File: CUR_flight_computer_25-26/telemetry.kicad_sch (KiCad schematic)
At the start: 19 parts, among them J14 Conn_Coaxial_Small, U5 E22-400MM_22S

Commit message: Apply MPNs for capacitors and connectors
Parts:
- C25: MPN (none) -> C0603C105K4RACTU
- C26, C27: value C_Small -> DNP; now not fitted; now left out of the parts list
- J14: value Conn_Coaxial_Small -> CON-SMA-EDGE-S; MPN (none) -> CON-SMA-EDGE-S
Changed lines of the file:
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@@
+			)
+		)
+		(property "MPN" "C0603C105K4RACTU"
+			(at 63.5 36.83 0)
+			(effects
+				(font
+					(size 1.27 1.27)
+				)
 			)
 		)
@@
 		(unit 1)
 		(exclude_from_sim no)
-		(in_bom yes)
-		(on_board yes)
-		(dnp no)
+		(in_bom no)
+		(on_board yes)
+		(dnp yes)
 		(fields_autoplaced yes)
 		(property "Reference" "C26"
@@
 			)
 		)
-		(property "Value" "C_Small"
+		(property "Value" "DNP"
 			(at 107.95 54.6162 0)
 			(effects
@@
 		(unit 1)
 		(exclude_from_sim no)
-		(in_bom yes)
-		(on_board yes)
-		(dnp no)
+		(in_bom no)
+		(on_board yes)
+		(dnp yes)
 		(fields_autoplaced yes)
 		(property "Reference" "C27"
@@
 			)
 		)
-		(property "Value" "C_Small"
+		(property "Value" "DNP"
 			(at 121.92 54.6162 0)
 			(effects
@@
 			)
 		)
-		(property "Value" "Conn_Coaxial_Small"
+		(property "Value" "CON-SMA-EDGE-S"
 			(at 130.2904 45.72 0)
 			(effects
@@
 			)
 		)
+		(property "MPN" "CON-SMA-EDGE-S"
+			(at 130.81 49.53 0)
+			(effects
+				(font
+					(size 1.27 1.27)
+				)
+			)
+		)

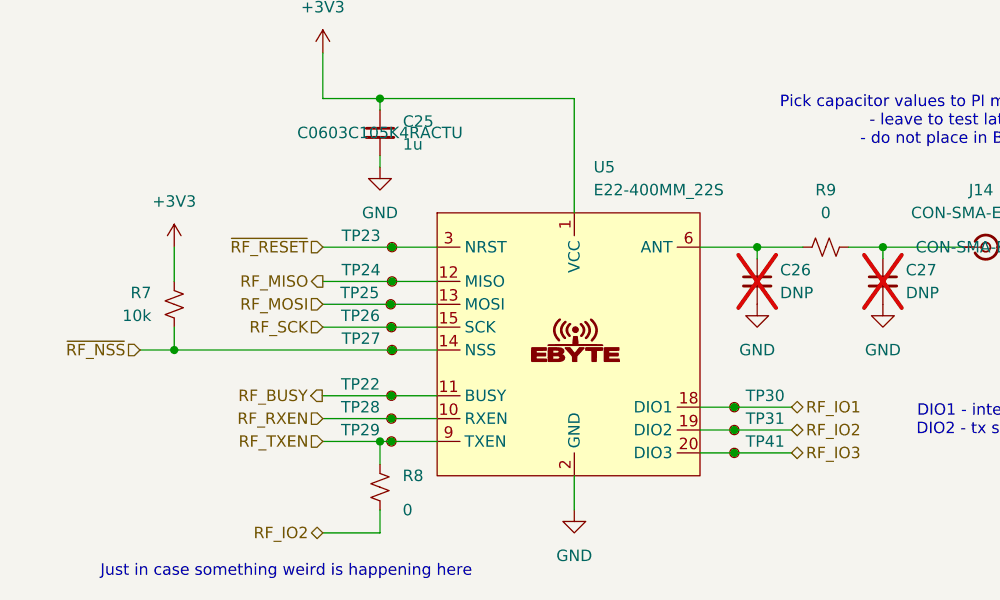
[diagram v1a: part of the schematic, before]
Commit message: Add MPNs for ICs
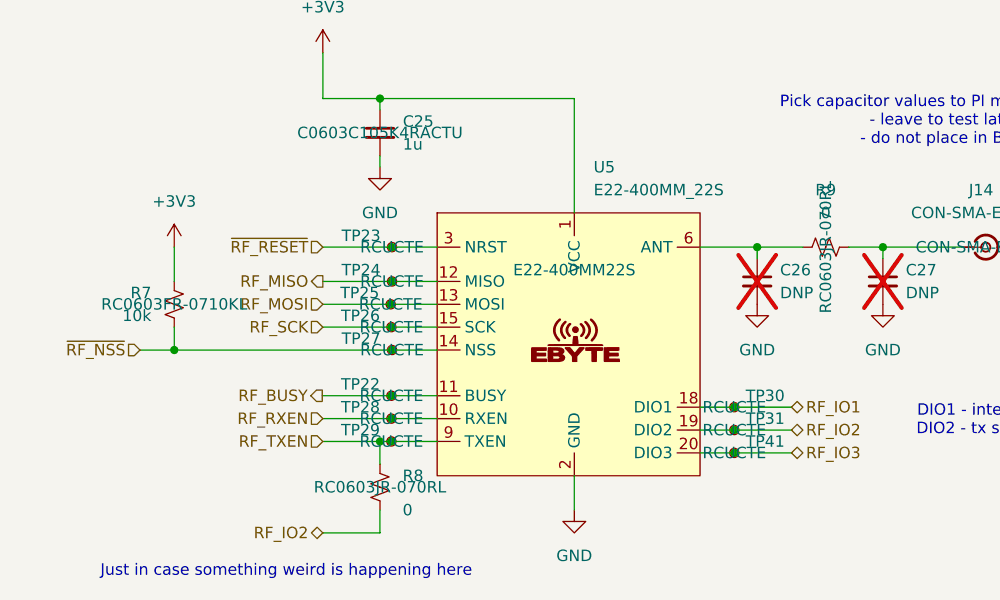
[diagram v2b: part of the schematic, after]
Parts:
- R7: MPN (none) -> RC0603FR-0710KL
- R8, R9: MPN (none) -> RC0603JR-070RL
- TP22, TP23, TP24, TP25, TP26, TP27, TP28, TP29, TP30, TP31, TP41: value TestPoint_Small -> RCUCTE; MPN (none) -> RCUCTE
- U5: MPN (none) -> E22-400MM22S
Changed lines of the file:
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@@
 			)
 		)
-		(property "Value" "TestPoint_Small"
+		(property "Value" "RCUCTE"
 			(at 63.5679 50.7999 0)
 			(effects
@@
 				)
 				(hide yes)
+			)
+		)
+		(property "MPN" "RCUCTE"
+			(at 64.8379 49.53 0)
+			(effects
+				(font
+					(size 1.27 1.27)
+				)
 			)
 		)
@@
 			)
 		)
-		(property "Value" "TestPoint_Small"
+		(property "Value" "RCUCTE"
 			(at 63.5 59.6899 0)
 			(effects
@@
 				)
 				(hide yes)
+			)
+		)
+		(property "MPN" "RCUCTE"
+			(at 64.77 58.42 0)
+			(effects
+				(font
+					(size 1.27 1.27)
+				)
 			)
 		)
@@
 			)
 		)
-		(property "Value" "TestPoint_Small"
+		(property "Value" "RCUCTE"
 			(at 63.5 67.3099 0)
 			(effects
@@
 				)
 				(hide yes)
+			)
+		)
+		(property "MPN" "RCUCTE"
+			(at 64.77 66.04 0)
+			(effects
+				(font
+					(size 1.27 1.27)
+				)
 			)
 		)
@@
 			)
 		)
-		(property "Value" "TestPoint_Small"
+		(property "Value" "RCUCTE"
 			(at 63.5 72.3899 0)
 			(effects
@@
 				)
 				(hide yes)
+			)
+		)
+		(property "MPN" "RCUCTE"
+			(at 64.77 71.12 0)
+			(effects
+				(font
+					(size 1.27 1.27)
+				)
 			)
 		)
@@
 			)
 		)
+		(property "MPN" "RC0603JR-070RL"
+			(at 63.5 76.2 0)
+			(effects
+				(font
+					(size 1.27 1.27)
+				)
+			)
+		)
 		(pin "1"
 		)
@@
 			)
 		)
-		(property "Value" "TestPoint_Small"
+		(property "Value" "RCUCTE"
 			(at 63.5 69.8499 0)
 			(effects
@@
 				)
 				(hide yes)
+			)
+		)
+		(property "MPN" "RCUCTE"
+			(at 64.77 68.58 0)
+			(effects
+				(font
+					(size 1.27 1.27)
+				)
 			)
 		)
@@
 			)
 		)
-		(property "Value" "TestPoint_Small"
+		(property "Value" "RCUCTE"
 			(at 104.14 71.1199 0)
 			(effects
@@
 			)
 		)
+		(property "MPN" "RCUCTE"
+			(at 102.87 69.85 0)
+			(effects
+				(font
+					(size 1.27 1.27)
+				)
+			)
+		)
 		(pin "1"
 		)
@@
 			)
 		)
-		(property "Value" "TestPoint_Small"
+		(property "Value" "RCUCTE"
 			(at 104.14 73.6599 0)
 			(effects
@@
 			)
 		)
+		(property "MPN" "RCUCTE"
+			(at 102.87 72.39 0)
+			(effects
+				(font
+					(size 1.27 1.27)
+				)
+			)
+		)
 		(pin "1"
 		)
@@
 			)
 		)
+		(property "MPN" "RC0603JR-070RL"
+			(at 113.03 49.53 0)
+			(effects
+				(font
+					(size 1.27 1.27)
+				)
+			)
+		)
 		(pin "1"
 		)
@@
 				)
 				(hide yes)
+			)
+		)
+		(property "MPN" "E22-400MM22S"
+			(at 85.09 52.07 0)
+			(effects
+				(font
+					(size 1.27 1.27)
+				)
 			)
 		)
@@
 			)
 		)
-		(property "Value" "TestPoint_Small"
+		(property "Value" "RCUCTE"
 			(at 63.5679 54.6099 0)
 			(effects
@@
 				)
 				(hide yes)
+			)
+		)
+		(property "MPN" "RCUCTE"
+			(at 64.8379 53.34 0)
+			(effects
+				(font
+					(size 1.27 1.27)
+				)
 			)
 		)
@@
 			)
 		)
-		(property "Value" "TestPoint_Small"
+		(property "Value" "RCUCTE"
 			(at 63.423 57.1499 0)
 			(effects
@@
 			)
 		)
+		(property "MPN" "RCUCTE"
+			(at 64.693 55.88 0)
+			(effects
+				(font
+					(size 1.27 1.27)
+				)
+			)
+		)
 		(pin "1"
 		)
@@
 			)
 		)
-		(property "Value" "TestPoint_Small"
+		(property "Value" "RCUCTE"
 			(at 104.14 68.5799 0)
 			(effects
@@
 			)
 		)
+		(property "MPN" "RCUCTE"
+			(at 102.87 67.31 0)
+			(effects
+				(font
+					(size 1.27 1.27)
+				)
+			)
+		)
 		(pin "1"
 		)
@@
 				)
 				(hide yes)
+			)
+		)
+		(property "MPN" "RC0603FR-0710KL"
+			(at 40.64 55.88 0)
+			(effects
+				(font
+					(size 1.27 1.27)
+				)
 			)
 		)
@@
 			)
 		)
-		(property "Value" "TestPoint_Small"
+		(property "Value" "RCUCTE"
 			(at 63.5679 62.2299 0)
 			(effects
@@
 			)
 		)
+		(property "MPN" "RCUCTE"
+			(at 64.8379 60.96 0)
+			(effects
+				(font
+					(size 1.27 1.27)
+				)
+			)
+		)

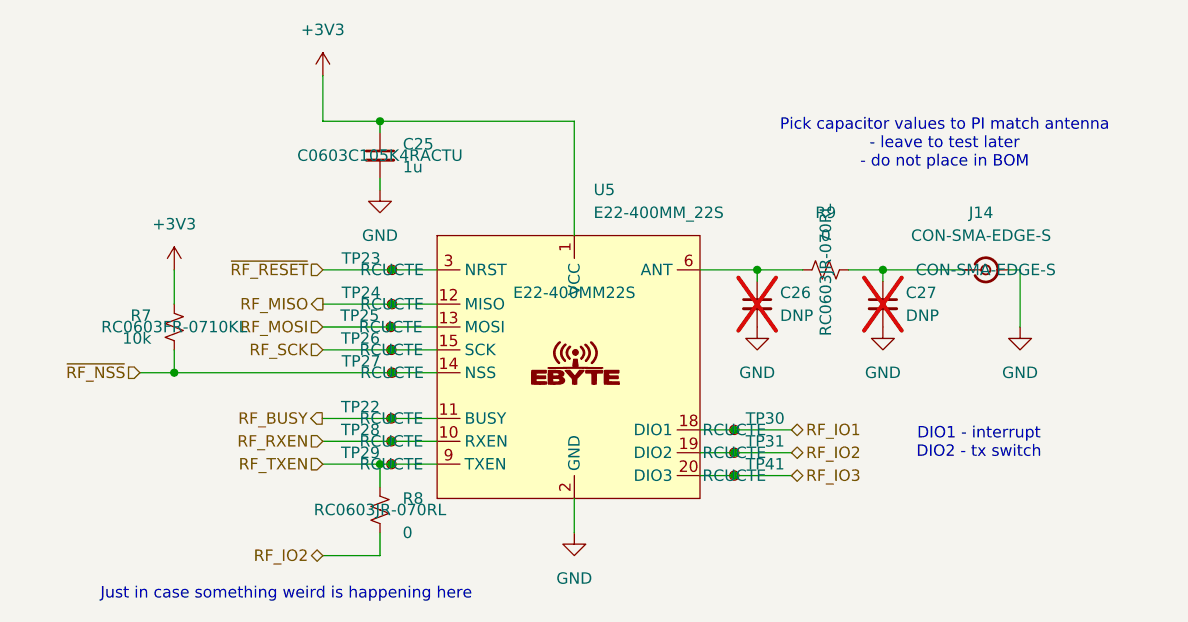
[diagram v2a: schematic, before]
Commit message: Hide MPNs
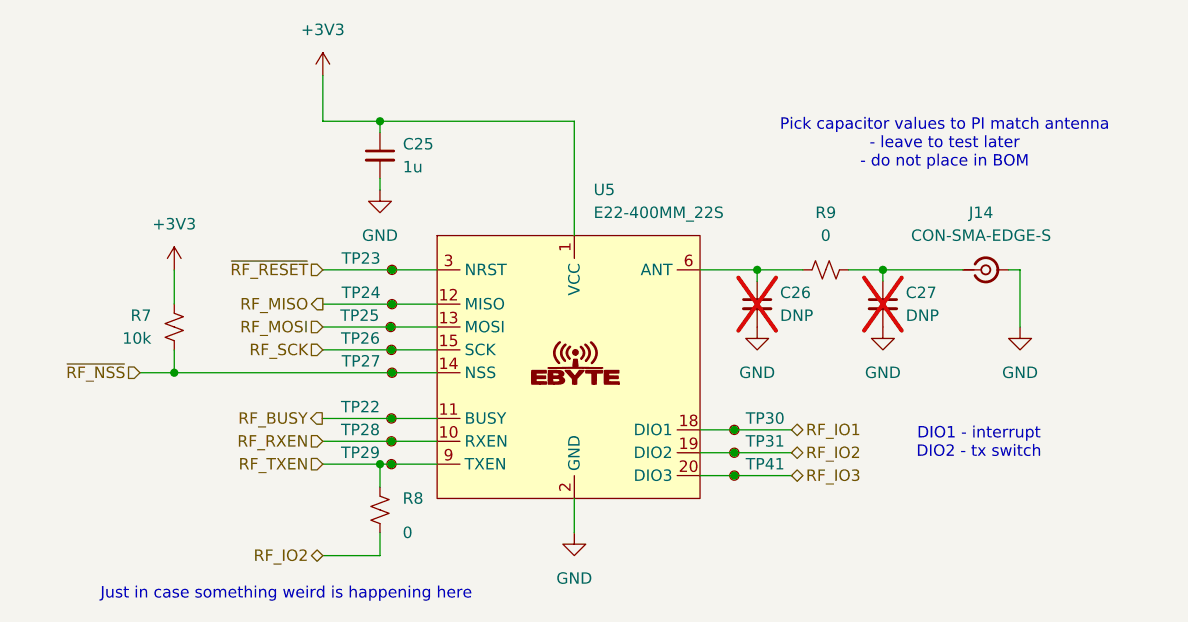
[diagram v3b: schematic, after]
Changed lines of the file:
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@@
 					(size 1.27 1.27)
 				)
+				(hide yes)
 			)
 		)
@@
 					(size 1.27 1.27)
 				)
+				(hide yes)
 			)
 		)
@@
 					(size 1.27 1.27)
 				)
+				(hide yes)
 			)
 		)
@@
 					(size 1.27 1.27)
 				)
+				(hide yes)
 			)
 		)
@@
 					(size 1.27 1.27)
 				)
+				(hide yes)
 			)
 		)
@@
 					(size 1.27 1.27)
 				)
+				(hide yes)
 			)
 		)
@@
 					(size 1.27 1.27)
 				)
+				(hide yes)
 			)
 		)
@@
 					(size 1.27 1.27)
 				)
+				(hide yes)
 			)
 		)
@@
 					(size 1.27 1.27)
 				)
+				(hide yes)
 			)
 		)
@@
 					(size 1.27 1.27)
 				)
+				(hide yes)
 			)
 		)
@@
 					(size 1.27 1.27)
 				)
+				(hide yes)
 			)
 		)
@@
 					(size 1.27 1.27)
 				)
+				(hide yes)
 			)
 		)
@@
 					(size 1.27 1.27)
 				)
+				(hide yes)
 			)
 		)
@@
 					(size 1.27 1.27)
 				)
+				(hide yes)
 			)
 		)
@@
 					(size 1.27 1.27)
 				)
+				(hide yes)
 			)
 		)
@@
 					(size 1.27 1.27)
 				)
+				(hide yes)
 			)
 		)
@@
 					(size 1.27 1.27)
 				)
-			)
-		)
+				(hide yes)
+			)
+		)

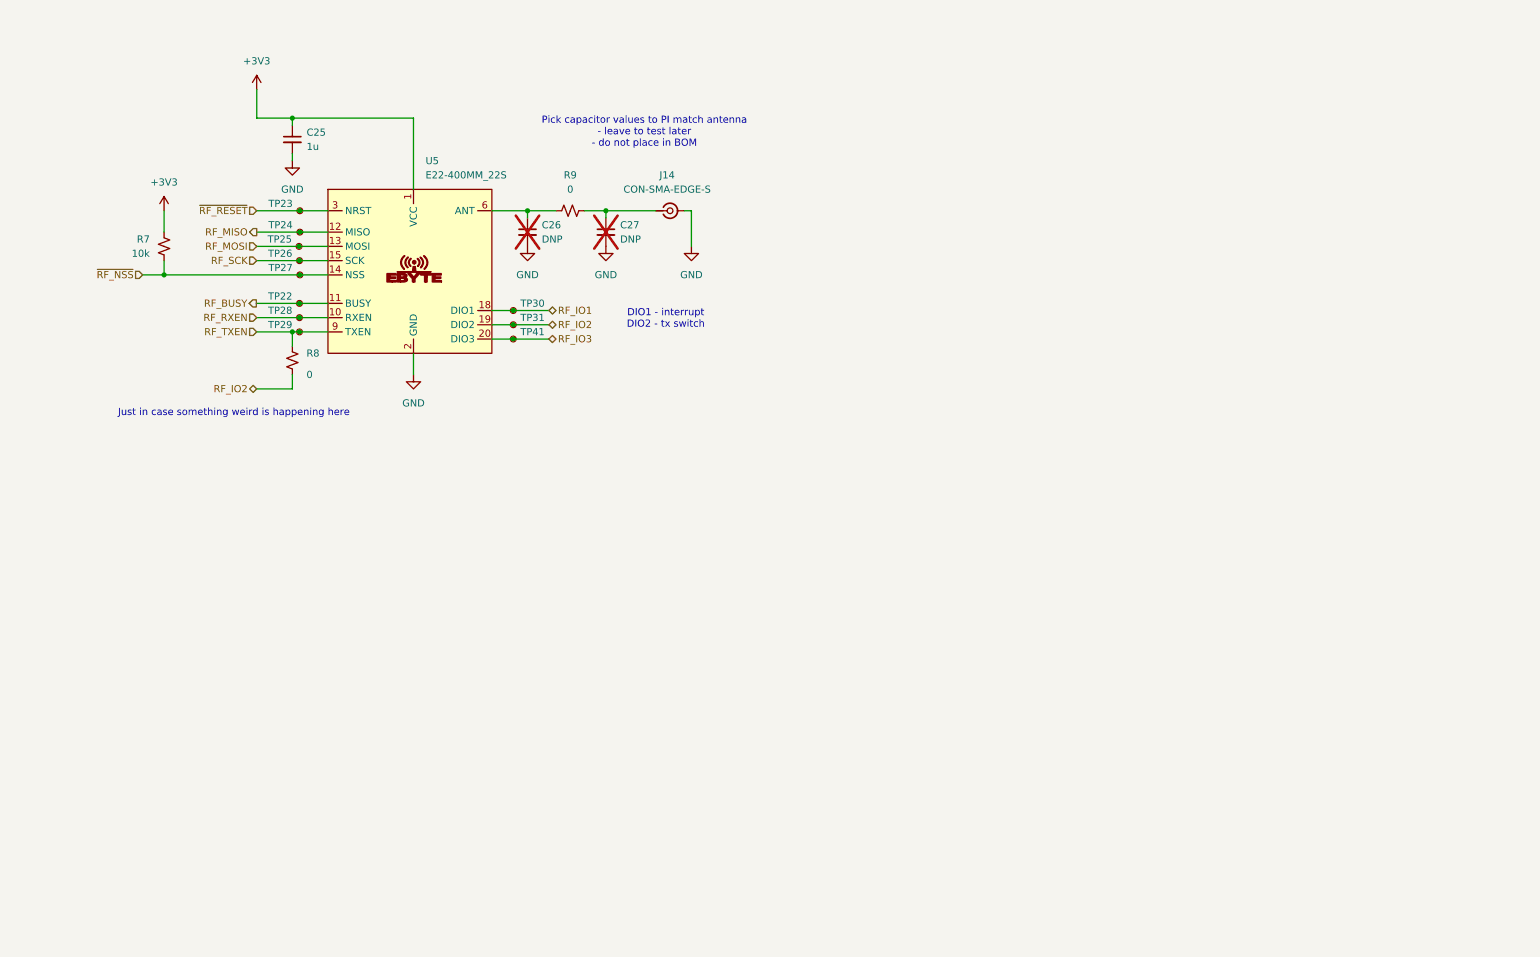
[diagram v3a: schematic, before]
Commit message: Cleaned up schematic
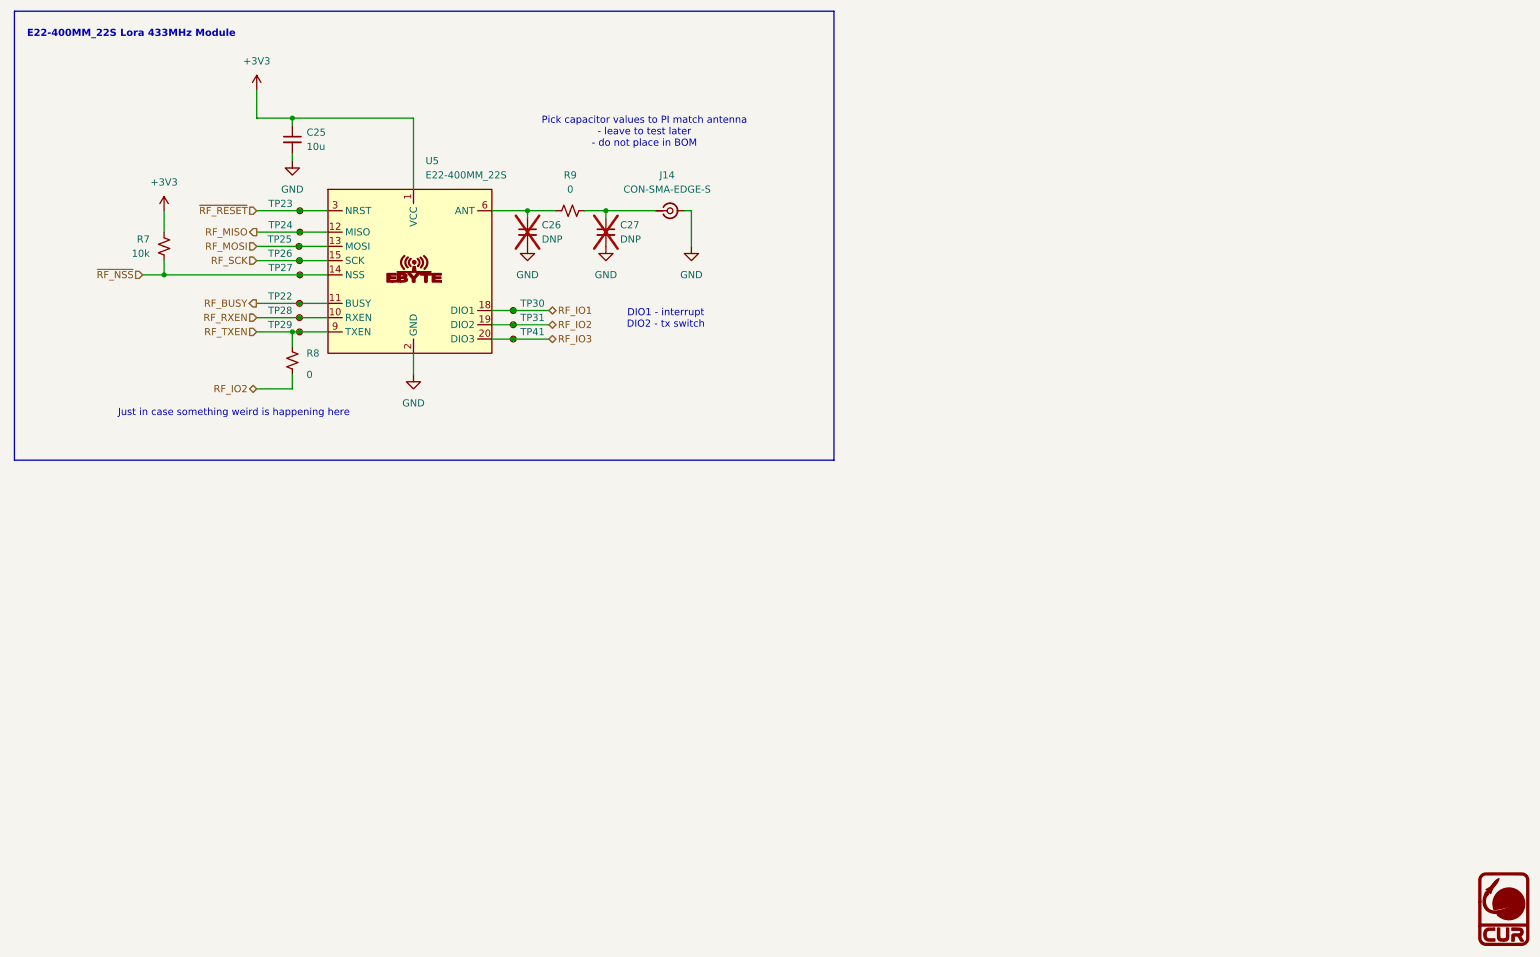
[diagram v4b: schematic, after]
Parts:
- C25: value 1u -> 10u
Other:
- note added: "E22-400MM_22S Lora 433MHz Module"
- company: (none) -> Clarkson University Rocketry
- title: (none) -> Flight Computer
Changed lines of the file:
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@@
 	(generator_version "9.0")
 	(paper "A4")
+	(title_block
+		(title "Flight Computer")
+		(date "2026-03-18")
+		(company "Clarkson University Rocketry")
+	)
+	(rectangle
+		(start 13.97 13.97)
+		(end 160.02 93.98)
+		(stroke
+			(width 0)
+			(type default)
+		)
+		(fill
+			(type none)
+		)
+	)
 	(text "Pick capacitor values to PI match antenna\n- leave to test later\n- do not place in BOM\n"
 		(exclude_from_sim no)
@@
 			(font
 				(size 1.27 1.27)
+			)
+		)
+	)
+	(text "E22-400MM_22S Lora 433MHz Module"
+		(exclude_from_sim no)
+		(at 34.798 18.034 0)
+		(effects
+			(font
+				(size 1.27 1.27)
+				(thickness 0.254)
+				(bold yes)
 			)
 		)
@@
 	)
 	(symbol
+		(lib_id "CUR_Logo:LOGO")
+		(at 279.4 173.99 0)
+		(unit 1)
+		(exclude_from_sim no)
+		(in_bom yes)
+		(on_board yes)
+		(dnp no)
+		(fields_autoplaced yes)
+		(property "Reference" "#G5"
+			(at 279.4 167.002 0)
+			(effects
+				(font
+					(size 1.27 1.27)
+				)
+				(hide yes)
+			)
+		)
+		(property "Value" "LOGO"
+			(at 279.4 180.978 0)
+			(effects
+				(font
+					(size 1.27 1.27)
+				)
+				(hide yes)
+			)
+		)
+		(property "Footprint" ""
+			(at 279.4 173.99 0)
+			(effects
+				(font
+					(size 1.27 1.27)
+				)
+				(hide yes)
+			)
+		)
+		(property "Datasheet" ""
+			(at 279.4 173.99 0)
+			(effects
+				(font
+					(size 1.27 1.27)
+				)
+				(hide yes)
+			)
+		)
+		(property "Description" ""
+			(at 279.4 173.99 0)
+			(effects
+				(font
+					(size 1.27 1.27)
+				)
+				(hide yes)
+			)
+		)
+		(instances
+			(project "CUR_flight_computer_25-26"
+				(path "/bf7761cc-1b32-4d86-809c-5f027005229b/16b7f3d3-745f-44d9-93a4-41f5bfd830cb"
+					(reference "#G5")
+					(unit 1)
+				)
+			)
+		)
+	)
+	(symbol
 		(lib_id "power:GND")
 		(at 63.5 40.64 0)
@@
 			)
 		)
-		(property "Value" "1u"
+		(property "Value" "10u"
 			(at 66.04 38.1062 0)
 			(effects

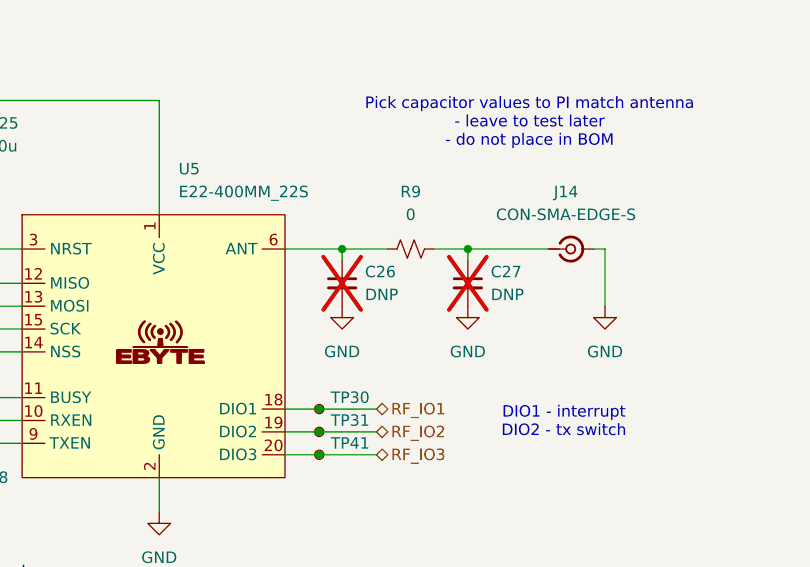
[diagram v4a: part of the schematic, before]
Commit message: BOM optimize 4.7u to 10u caps
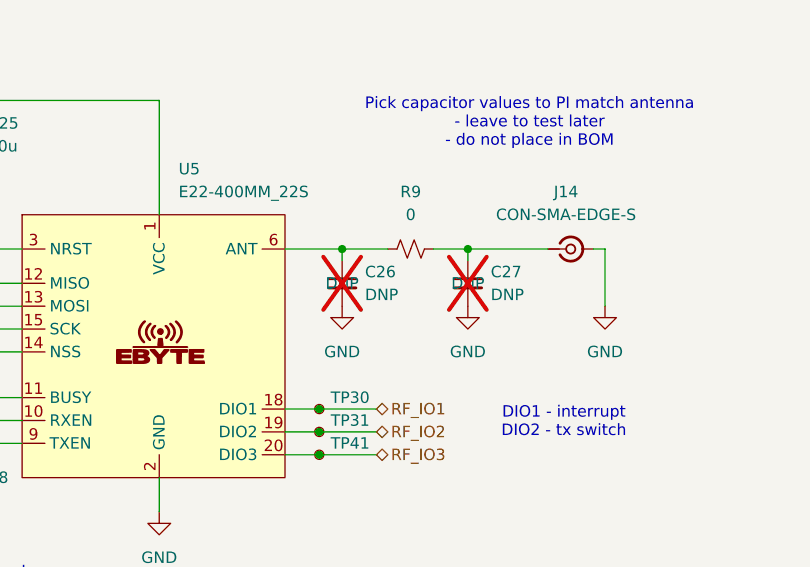
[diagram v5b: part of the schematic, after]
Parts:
- C25: MPN C0603C105K4RACTU -> LMK107BBJ106MALT
- C26, C27: MPN (none) -> DNP
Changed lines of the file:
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@@
 			)
 		)
-		(property "MPN" "C0603C105K4RACTU"
+		(property "MPN" "LMK107BBJ106MALT"
 			(at 63.5 36.83 0)
 			(effects
@@
 			)
 		)
+		(property "MPN" "DNP"
+			(at 105.41 53.34 0)
+			(effects
+				(font
+					(size 1.27 1.27)
+				)
+			)
+		)
 		(pin "2"
 		)
@@
 			)
 		)
+		(property "MPN" "DNP"
+			(at 119.38 53.34 0)
+			(effects
+				(font
+					(size 1.27 1.27)
+				)
+			)
+		)
